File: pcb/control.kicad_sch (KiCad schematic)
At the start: 5 parts

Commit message: Label parts for JLCPCB
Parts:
- CR5: LCSC (none) -> C20345394
- renumbered BLUETOOTH0 to BT_EN0, STORAGE0 to STORAGE_EN0, TRANSLATION0 to TRANSLATION_EN0
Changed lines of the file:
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@@
 		(dnp no)
 		(fields_autoplaced yes)
-		(property "Reference" "#PWR020"
+		(property "Reference" "#PWR034"
 			(at 139.7 80.01 0)
 			(effects
@@
 		(dnp no)
 		(fields_autoplaced yes)
-		(property "Reference" "TRANSLATION0"
+		(property "Reference" "TRANSLATION_EN0"
 			(at 168.91 38.1 0)
 			(effects
@@
 		(dnp no)
 		(fields_autoplaced yes)
-		(property "Reference" "#PWR025"
+		(property "Reference" "#PWR06"
 			(at 63.5 49.53 0)
 			(effects
@@
 		(dnp no)
 		(fields_autoplaced yes)
-		(property "Reference" "STORAGE0"
+		(property "Reference" "STORAGE_EN0"
 			(at 167.64 59.69 0)
 			(effects
@@
 		(dnp no)
 		(fields_autoplaced yes)
-		(property "Reference" "#PWR0127"
+		(property "Reference" "#PWR014"
 			(at 175.26 76.2 0)
 			(effects
@@
 		(dnp no)
 		(fields_autoplaced yes)
-		(property "Reference" "#PWR024"
+		(property "Reference" "#PWR032"
 			(at 73.66 54.61 0)
 			(effects
@@
 			)
 		)
+		(property "LCSC" "C20345394"
+			(at 184.15 64.77 0)
+			(effects
+				(font
+					(size 1.27 1.27)
+				)
+				(hide yes)
+			)
+		)
 		(pin "2"
 		)
@@
 		)
 		(instances
+			(project "stenoswitch"
+				(path "/06a6eca0-edda-4cc0-a23f-017602e67f07/99f3b279-b2b0-4dd5-ab05-9b518546ce95/93dd658d-093b-457b-aa9d-06e2289958ef"
+					(reference "CR5")
+					(unit 1)
+				)
+			)
 			(project "right_hand"
 				(path "/efcccfe8-5e20-4b1b-8d3b-61fce771481e/93dd658d-093b-457b-aa9d-06e2289958ef"
@@
 		(dnp no)
 		(fields_autoplaced yes)
-		(property "Reference" "BLUETOOTH0"
+		(property "Reference" "BT_EN0"
 			(at 167.64 80.01 0)
 			(effects
@@
 		(dnp no)
 		(fields_autoplaced yes)
-		(property "Reference" "#PWR026"
+		(property "Reference" "#PWR033"
 			(at 142.24 59.69 0)
 			(effects
@@
 		(dnp no)
 		(fields_autoplaced yes)
-		(property "Reference" "#PWR0128"
+		(property "Reference" "#PWR00"
 			(at 175.26 96.52 0)
 			(effects
@@
 		(dnp no)
 		(fields_autoplaced yes)
-		(property "Reference" "#PWR022"
+		(property "Reference" "#PWR011"
 			(at 69.85 74.93 0)
 			(effects
@@
 		(dnp no)
 		(fields_autoplaced yes)
-		(property "Reference" "#PWR0126"
+		(property "Reference" "#PWR015"
 			(at 176.53 54.61 0)
 			(effects
@@
 		(dnp no)
 		(fields_autoplaced yes)
-		(property "Reference" "#PWR030"
+		(property "Reference" "#PWR0101"
 			(at 194.31 71.12 0)
 			(effects
@@
 		)
 		(instances
-			(project "right_hand"
-				(path "/efcccfe8-5e20-4b1b-8d3b-61fce771481e/93dd658d-093b-457b-aa9d-06e2289958ef"
+			(project "stenoswitch"
+				(path "/06a6eca0-edda-4cc0-a23f-017602e67f07/99f3b279-b2b0-4dd5-ab05-9b518546ce95/93dd658d-093b-457b-aa9d-06e2289958ef"
+					(reference "#PWR0101")
+					(unit 1)
+				)
+			)
+			(project "right_hand"
+				(path "/efcccfe8-5e20-4b1b-8d3b-61fce771481e/93dd658d-093b-457b-aa9d-06e2289958ef"

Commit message: Add DNP for right hand
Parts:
- A1: now not fitted
- BLUETOOTH0: renamed from BT_EN0; now not fitted
- STORAGE0: renamed from STORAGE_EN0; now not fitted
- TRANSLATION0: renamed from TRANSLATION_EN0; now not fitted
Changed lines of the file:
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@@
 		(dnp no)
 		(fields_autoplaced yes)
-		(property "Reference" "#PWR034"
+		(property "Reference" "#PWR020"
 			(at 139.7 80.01 0)
 			(effects
@@
 		(in_bom yes)
 		(on_board yes)
-		(dnp no)
-		(fields_autoplaced yes)
-		(property "Reference" "TRANSLATION_EN0"
+		(dnp yes)
+		(fields_autoplaced yes)
+		(property "Reference" "TRANSLATION0"
 			(at 168.91 38.1 0)
 			(effects
@@
 		(dnp no)
 		(fields_autoplaced yes)
-		(property "Reference" "#PWR06"
+		(property "Reference" "#PWR025"
 			(at 63.5 49.53 0)
 			(effects
@@
 		(in_bom yes)
 		(on_board yes)
-		(dnp no)
-		(fields_autoplaced yes)
-		(property "Reference" "STORAGE_EN0"
+		(dnp yes)
+		(fields_autoplaced yes)
+		(property "Reference" "STORAGE0"
 			(at 167.64 59.69 0)
 			(effects
@@
 		(dnp no)
 		(fields_autoplaced yes)
-		(property "Reference" "#PWR014"
+		(property "Reference" "#PWR0127"
 			(at 175.26 76.2 0)
 			(effects
@@
 		(dnp no)
 		(fields_autoplaced yes)
-		(property "Reference" "#PWR032"
+		(property "Reference" "#PWR024"
 			(at 73.66 54.61 0)
 			(effects
@@
 		(in_bom yes)
 		(on_board yes)
-		(dnp no)
-		(fields_autoplaced yes)
-		(property "Reference" "BT_EN0"
+		(dnp yes)
+		(fields_autoplaced yes)
+		(property "Reference" "BLUETOOTH0"
 			(at 167.64 80.01 0)
 			(effects
@@
 		(in_bom yes)
 		(on_board yes)
-		(dnp no)
+		(dnp yes)
 		(fields_autoplaced yes)
 		(property "Reference" "A1"
@@
 		(dnp no)
 		(fields_autoplaced yes)
-		(property "Reference" "#PWR033"
+		(property "Reference" "#PWR026"
 			(at 142.24 59.69 0)
 			(effects
@@
 		(dnp no)
 		(fields_autoplaced yes)
-		(property "Reference" "#PWR00"
+		(property "Reference" "#PWR0128"
 			(at 175.26 96.52 0)
 			(effects
@@
 		(dnp no)
 		(fields_autoplaced yes)
-		(property "Reference" "#PWR011"
+		(property "Reference" "#PWR022"
 			(at 69.85 74.93 0)
 			(effects
@@
 		(dnp no)
 		(fields_autoplaced yes)
-		(property "Reference" "#PWR015"
+		(property "Reference" "#PWR0126"
 			(at 176.53 54.61 0)
 			(effects
@@
 		(dnp no)
 		(fields_autoplaced yes)
-		(property "Reference" "#PWR0101"
+		(property "Reference" "#PWR030"
 			(at 194.31 71.12 0)
 			(effects

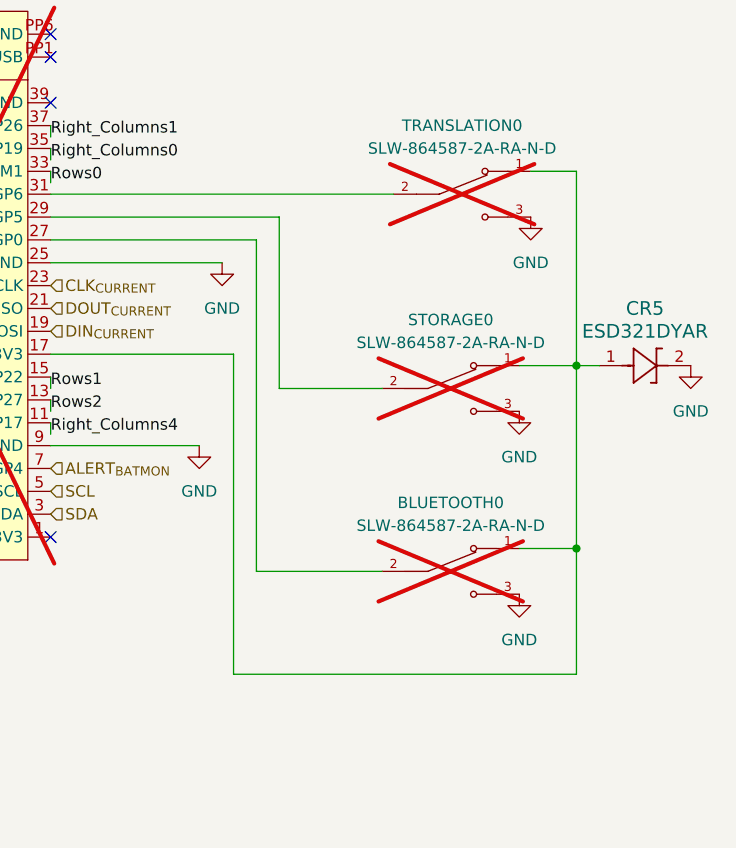
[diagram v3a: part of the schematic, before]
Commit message: Create right hand order for JLCPCB
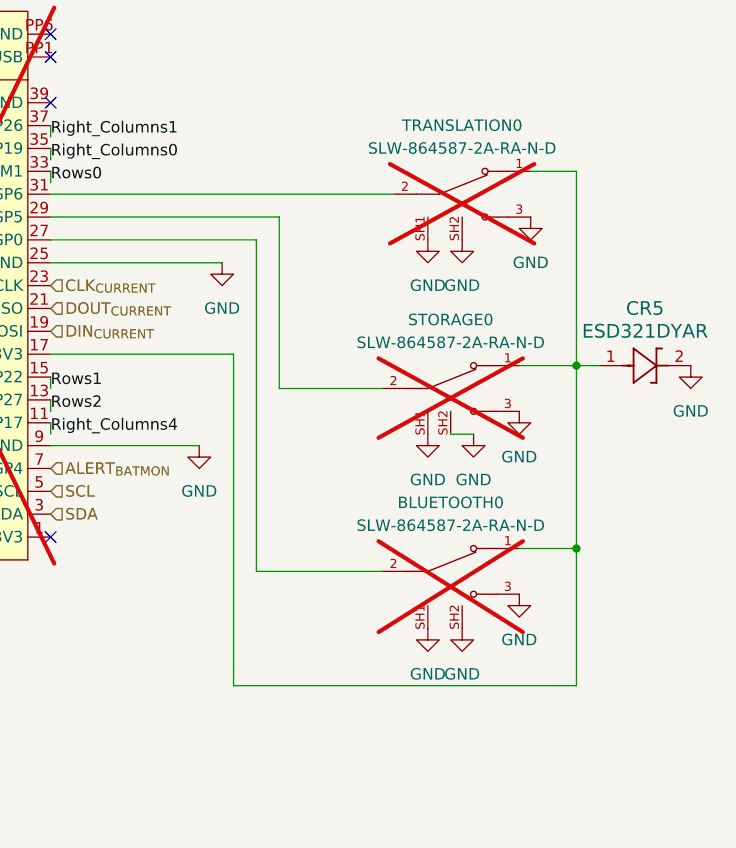
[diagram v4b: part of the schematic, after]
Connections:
- net GND: now also BLUETOOTH0.SH1, BLUETOOTH0.SH2, STORAGE0.SH1, STORAGE0.SH2, TRANSLATION0.SH1, TRANSLATION0.SH2
